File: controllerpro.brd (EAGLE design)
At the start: 38.7 x 83.2 mm, 10 parts, among them IC1 MCP1703CB, IC2 741G3157DBVR, IC3 741G3157DBVR, IC4 741G3157DBVR, IC5 741G3157DBVR

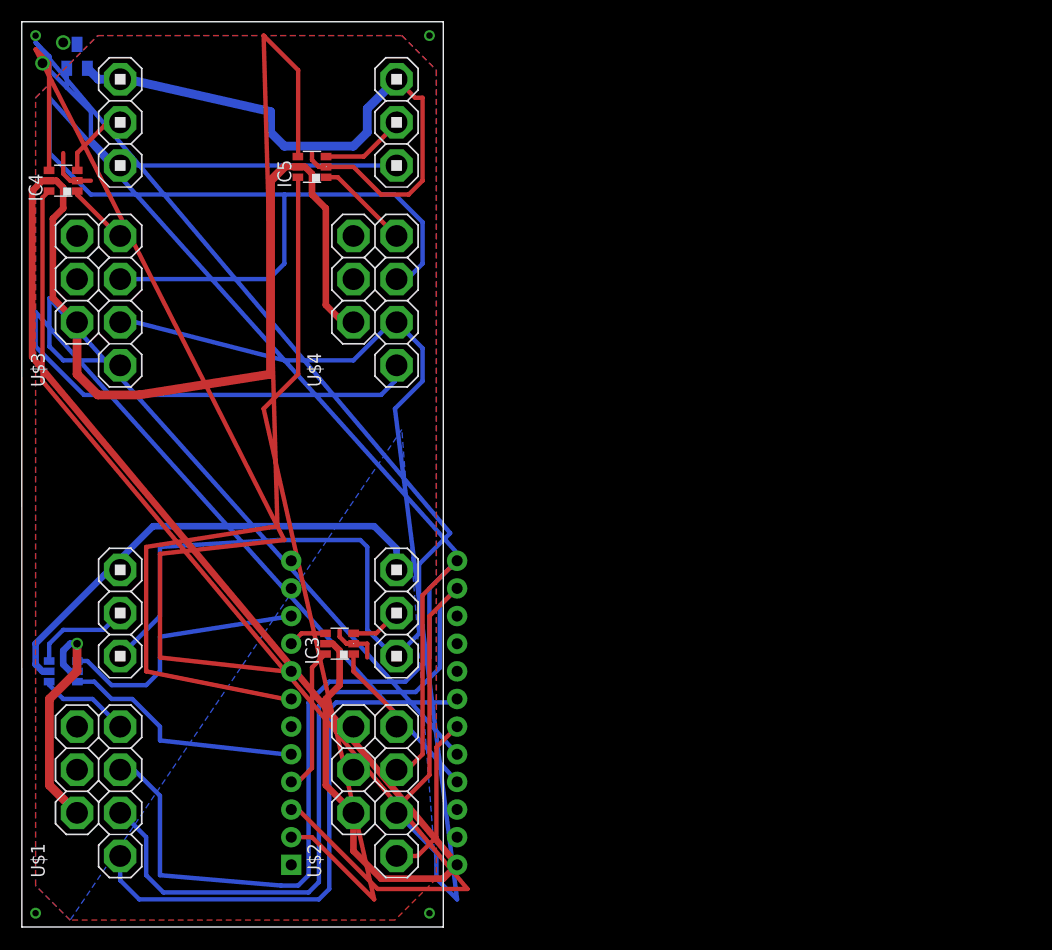
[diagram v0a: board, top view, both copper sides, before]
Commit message: Teensy in the middle of 2x2 (rotated)
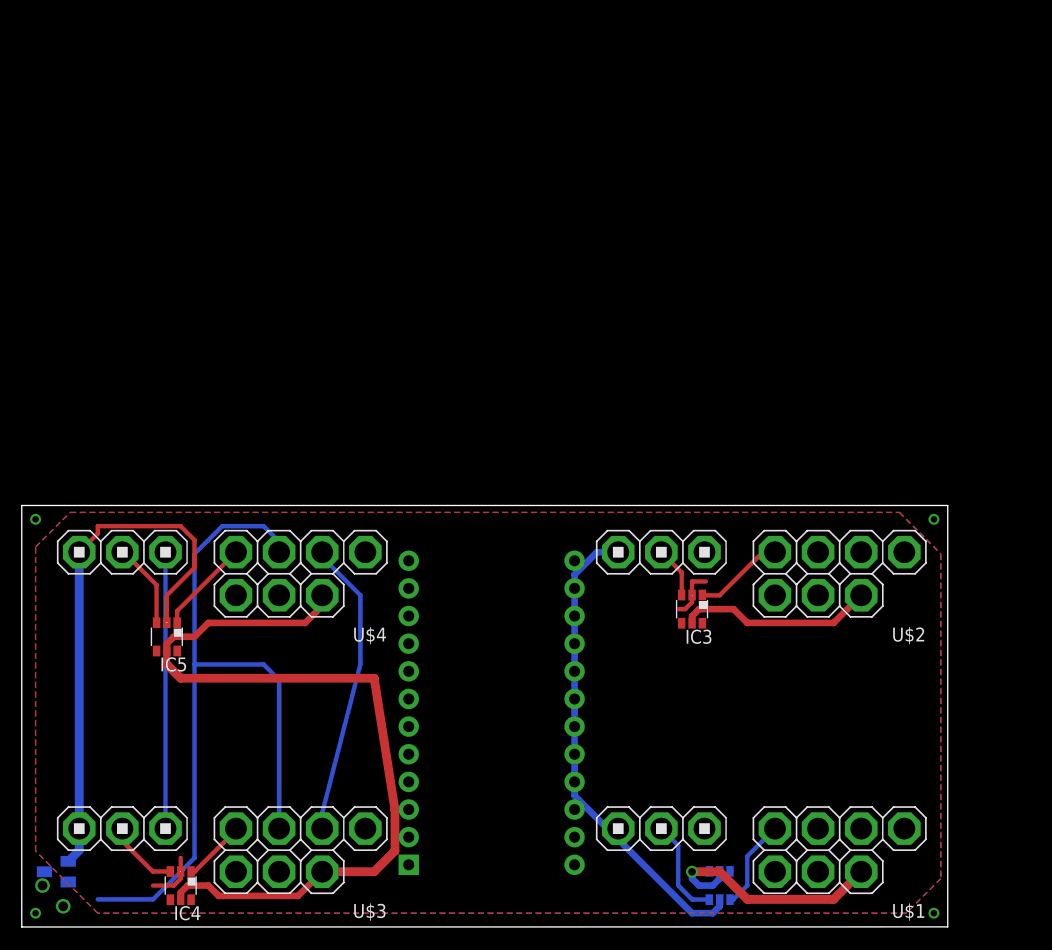
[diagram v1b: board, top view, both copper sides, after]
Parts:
- moved IC1 75.0 mm to (3.17, 5.08), turned to 270 degrees
- moved IC4 65.7 mm to (14.6, 3.81), turned to 180 degrees
- moved U$1 65.5 mm to (69.2, 5.08), turned to 180 degrees
- moved IC2 63.5 mm to (64.1, 3.81), turned to 0 degrees
- moved U$3 60.2 mm to (19.7, 5.08), turned to 180 degrees
- moved IC5 45.2 mm to (13.3, 26.7), turned to 180 degrees
- moved U$2 40.6 mm to (69.2, 30.5), turned to 180 degrees
- moved U$4 34.7 mm to (19.7, 30.5), turned to 180 degrees
- moved IC3 32.5 mm to (61.6, 29.2), turned to 180 degrees
- moved U$5 10.8 mm to (43.2, 19.7)
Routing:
- net CLOCK: track 176.4 -> 27.3 mm
- net LATCH: track 215.3 -> 70.8 mm
- net V33: track 156.4 -> 25.4 mm
- net S_OR_NES3: track 98.1 -> 0.00 mm
- net N64_OR_NES2: track 97.8 -> 0.00 mm
- net DATA2: track 95.3 -> 0.00 mm
- net DATA3: track 94.8 -> 0.00 mm
- net VCC: track 209.9 -> 117.3 mm
- net N64_OR_NES3: track 78.8 -> 0.00 mm
- net S_OR_NES2: track 67.9 -> 0.00 mm
- net S_OR_NES0: track 51.2 -> 0.00 mm
- net DATA0: track 24.4 -> 0.00 mm
- net N64_OR_NES0: track 22.7 -> 0.00 mm
- net S_OR_NES1: track 15.3 -> 0.00 mm
- net N64_OR_NES1: track 13.4 -> 0.00 mm
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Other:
- board size 38.7 x 83.2 mm -> 85.1 x 38.7 mm

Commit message: Using only needed pins
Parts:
- U$5: value TEENSY_HEADERS -> TEENSY_MC_PINS; device custom:TEENSY_HEADERS -> custom:TEENSY_MC_PINS
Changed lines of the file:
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@@
 <element name="IC4" library="74xx-little-de" package="DBV_R-PDSO-G6" value="741G3157DBVR" x="14.605" y="3.81" rot="R180"/>
 <element name="IC5" library="74xx-little-de" package="DBV_R-PDSO-G6" value="741G3157DBVR" x="13.335" y="26.67" rot="R180"/>
-<element name="U$5" library="custom" package="TEENSY_HEADERS" value="TEENSY_HEADERS" x="43.18" y="19.685" rot="MR90"/>
+<element name="U$5" library="custom" package="TEENSY_MC_PINS" value="TEENSY_MC_PINS" x="43.18" y="19.685" rot="MR90"/>
 </elements>
 <signals>

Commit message: All wired up (intially)!
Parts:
- moved IC1 39.4 mm to (42.5, 6.35), flipped to the top
- moved IC4 14.3 mm to (27.9, 8.89), turned to 270 degrees
- moved IC2 8.54 mm to (70.5, 9.53), flipped to the top
- moved IC3 5.43 mm to (56.5, 27.3), turned to 90 degrees
- moved U$1 4.96 mm to (66.0, 8.89), turned to 0 degrees
- moved U$3 4.96 mm to (16.5, 8.89), turned to 0 degrees
- moved U$2 3.24 mm to (68.6, 27.3)
- moved U$4 3.24 mm to (19.1, 27.3)
- moved IC5 0.90 mm to (14.0, 26.0)
- moved U$5 0.63 mm to (42.5, 19.7)
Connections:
- net DATA0: now also U$5.D2; no longer U$5.D3
- net DATA1: now also U$5.D3; no longer U$5.D2
- net DATA2: now also U$5.D0; no longer U$5.D1
- net DATA3: now also U$5.D1; no longer U$5.D0
- net N64_OR_NES0: now also U$5.B2; no longer U$5.B3
- net N64_OR_NES1: now also U$5.B3; no longer U$5.B2
- net N64_OR_NES2: now also U$5.B0; no longer U$5.B1
- net N64_OR_NES3: now also U$5.B1; no longer U$5.B0
- net S_OR_NES0: now also U$5.F6; no longer U$5.F7
- net S_OR_NES1: now also U$5.F7; no longer U$5.F6
- net S_OR_NES2: now also U$5.F4; no longer U$5.F5
- net S_OR_NES3: now also U$5.F5; no longer U$5.F4
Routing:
- net V33: track 25.4 -> 183.7 mm
- net CLOCK: track 27.3 -> 149.8 mm, vias 0 -> 1
- net LATCH: track 70.8 -> 159.4 mm
- net GND: track 104.0 -> 25.8 mm, vias 0 -> 2
- net S_OR_NES2: track 0.00 -> 63.6 mm, vias 0 -> 2
- net DATA0: track 0.00 -> 48.4 mm, vias 0 -> 1
- net VCC: track 117.3 -> 74.6 mm
- net N64_OR_NES3: track 0.00 -> 39.7 mm
- net N64_OR_NES0: track 0.00 -> 38.8 mm, vias 0 -> 1
- net S_OR_NES1: track 0.00 -> 37.5 mm
- net S_OR_NES3: track 0.00 -> 25.6 mm, vias 0 -> 1
- net N64_OR_NES1: track 0.00 -> 24.6 mm
- net DATA3: track 0.00 -> 24.4 mm
- net DATA1: track 0.00 -> 22.5 mm
- net DATA2: track 0.00 -> 19.4 mm, vias 0 -> 2
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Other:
- board size 85.1 x 38.7 mm -> 84.5 x 37.5 mm

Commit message: Trying to actually line up box with board
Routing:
- net GND: track 25.8 -> 24.0 mm
- net V33: track 183.7 -> 184.4 mm
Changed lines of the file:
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@@
 <wire x1="0" y1="0" x2="84.455" y2="0.01" width="0" layer="20"/>
 <wire x1="84.455" y1="0.01" x2="84.455" y2="37.465" width="0" layer="20"/>
+<dimension x1="51.435" y1="5.715" x2="33.655" y2="5.715" x3="42.545" y3="-4.444996875" textsize="1.778" layer="48" unit="inch" precision="4"/>
+<dimension x1="16.51" y1="8.89" x2="33.655" y2="8.89" x3="25.0825" y3="-5.08" textsize="1.778" layer="48" unit="inch" precision="4"/>
+<dimension x1="66.04" y1="8.89" x2="51.435" y2="8.89" x3="58.7375" y3="-4.445" textsize="1.778" layer="48" unit="inch" precision="4"/>
+<dimension x1="66.04" y1="8.89" x2="84.455" y2="8.89" x3="75.2475" y3="-4.445" textsize="1.778" layer="48" unit="inch" precision="4"/>
+<dimension x1="16.51" y1="8.89" x2="0" y2="8.89" x3="8.255" y3="-4.445" textsize="1.778" layer="48" unit="inch" precision="4"/>
+<dimension x1="16.51" y1="8.89" x2="42.545" y2="8.89" x3="29.5275" y3="-12.7" textsize="1.778" layer="48" unit="inch" precision="4"/>
+<dimension x1="19.05" y1="27.305" x2="42.545" y2="27.305" x3="30.7975" y3="43.18" textsize="1.778" layer="48" unit="inch" precision="4"/>
+<dimension x1="66.04" y1="8.89" x2="42.545" y2="8.89" x3="54.2925" y3="-12.7" textsize="1.778" layer="48" dtype="vertical" unit="inch" precision="4"/>
+<dimension x1="68.58" y1="27.305" x2="42.545" y2="27.305" x3="55.5625" y3="43.18" textsize="1.778" layer="48" dtype="vertical" unit="inch" precision="4"/>
+<dimension x1="16.51" y1="8.89" x2="42.545" y2="18.7325" x3="26.035" y3="13.81125" textsize="1.778" layer="48" dtype="vertical" unit="inch" precision="4"/>
+<dimension x1="42.545" y1="18.7325" x2="68.58" y2="27.305" x3="56.515" y3="23.01875" textsize="1.778" layer="48" dtype="vertical" unit="inch" precision="4"/>
 </plain>
 <attributes>
@@
 <vertex x="83.185" y="34.29"/>
 </polygon>
-<wire x1="80.01" y1="6.35" x2="80.01" y2="5.3594" width="0.6096" layer="16"/>
-<wire x1="80.01" y1="5.3594" x2="80.4418" y2="4.9276" width="0.6096" layer="16"/>
-<wire x1="81.28" y1="5.08" x2="80.5942" y2="5.08" width="0.6096" layer="16"/>
-<wire x1="80.5942" y1="5.08" x2="80.4418" y2="4.9276" width="0.4064" layer="16"/>
 <contactref element="U$5" pad="GND"/>
 <wire x1="13.97" y1="27.325" x2="13.97" y2="29.21" width="0.8128" layer="1"/>
-<wire x1="54.1782" y1="31.2674" x2="54.1782" y2="30.9118" width="0.6096" layer="1"/>
-<wire x1="54.1782" y1="30.9118" x2="56.515" y2="28.575" width="0.6096" layer="1"/>
-<wire x1="56.515" y1="28.575" x2="56.515" y2="27.94" width="0.6096" layer="1"/>
-<wire x1="56.515" y1="27.94" x2="57.15" y2="27.305" width="0.6096" layer="1"/>
-<wire x1="57.15" y1="27.305" x2="57.805" y2="27.305" width="0.6096" layer="1"/>
 <wire x1="70.485" y1="8.235" x2="70.485" y2="6.985" width="0.6096" layer="1"/>
 <wire x1="70.485" y1="6.985" x2="69.85" y2="6.35" width="0.6096" layer="1"/>
 <wire x1="26.65" y1="8.89" x2="27.305" y2="8.89" width="0.6096" layer="1"/>
 <wire x1="27.305" y1="8.89" x2="27.94" y2="8.255" width="0.6096" layer="1"/>
-<wire x1="27.94" y1="8.255" x2="27.94" y2="7.62" width="0.6096" layer="1"/>
-<wire x1="27.94" y1="7.62" x2="30.48" y2="5.08" width="0.6096" layer="1"/>
-<wire x1="30.48" y1="5.08" x2="30.7594" y2="5.08" width="0.6096" layer="1"/>
-<wire x1="30.7594" y1="5.08" x2="30.9118" y2="4.9276" width="0.6096" layer="1"/>
 <via x="41.275" y="27.94" extent="1-16" drill="0.7"/>
 <via x="46.355" y="22.86" extent="1-16" drill="0.7"/>
 <wire x1="41.275" y1="27.94" x2="46.355" y2="22.86" width="0.6096" layer="16"/>
+<wire x1="27.94" y1="8.255" x2="27.94" y2="6.985" width="0.6096" layer="1"/>
+<wire x1="27.94" y1="6.985" x2="29.845" y2="5.08" width="0.6096" layer="1"/>
+<wire x1="29.845" y1="5.08" x2="30.6324" y2="5.08" width="0.6096" layer="1"/>
+<wire x1="30.6324" y1="5.08" x2="30.7848" y2="4.9276" width="0.6096" layer="1"/>
+<wire x1="57.805" y1="27.305" x2="57.15" y2="27.305" width="0.6096" layer="1"/>
+<wire x1="57.15" y1="27.305" x2="56.515" y2="27.94" width="0.6096" layer="1"/>
+<wire x1="56.515" y1="27.94" x2="56.515" y2="29.845" width="0.6096" layer="1"/>
+<wire x1="56.515" y1="29.845" x2="55.245" y2="31.115" width="0.6096" layer="1"/>
+<wire x1="55.245" y1="31.115" x2="54.4576" y2="31.115" width="0.6096" layer="1"/>
+<wire x1="54.4576" y1="31.115" x2="54.3052" y2="31.2674" width="0.6096" layer="1"/>
 </signal>
 <signal name="V33">
@@
 <contactref element="U$4" pad="5"/>
 <contactref element="IC1" pad="2"/>
-<wire x1="12.573" y1="31.2674" x2="12.5476" y2="31.2674" width="0.4064" layer="16"/>
-<wire x1="12.065" y1="30.48" x2="12.065" y2="21.59" width="0.6096" layer="16"/>
+<wire x1="12.065" y1="30.6324" x2="12.065" y2="21.59" width="0.6096" layer="16"/>
 <wire x1="12.065" y1="21.59" x2="1.5875" y2="11.1125" width="0.6096" layer="16"/>
 <wire x1="1.5875" y1="11.1125" x2="1.5875" y2="3.4925" width="0.6096" layer="16"/>
 <wire x1="1.5875" y1="3.4925" x2="3.4925" y2="1.5875" width="0.6096" layer="16"/>
 <wire x1="3.4925" y1="1.5875" x2="19.6469" y2="1.5875" width="0.6096" layer="16"/>
-<wire x1="19.6469" y1="1.5875" x2="22.987" y2="4.9276" width="0.6096" layer="16"/>
+<wire x1="19.6469" y1="1.5875" x2="22.86" y2="4.445" width="0.6096" layer="16"/>
+<wire x1="22.86" y1="4.445" x2="22.86" y2="4.9276" width="0.6096" layer="16"/>
 <wire x1="41.445" y1="5.4" x2="40.325" y2="5.4" width="0.6096" layer="1"/>
 <wire x1="40.325" y1="5.4" x2="37.465" y2="2.54" width="0.6096" layer="1"/>
 <wire x1="37.465" y1="2.54" x2="25.3746" y2="2.54" width="0.6096" layer="1"/>
-<wire x1="25.3746" y1="2.54" x2="22.987" y2="4.9276" width="0.6096" layer="1"/>
-<wire x1="62.103" y1="31.2674" x2="62.103" y2="30.988" width="0.6096" layer="16"/>
-<wire x1="62.103" y1="30.988" x2="59.69" y2="28.575" width="0.6096" layer="16"/>
-<wire x1="59.69" y1="28.575" x2="49.53" y2="28.575" width="0.6096" layer="16"/>
+<wire x1="25.3746" y1="2.54" x2="23.495" y2="4.445" width="0.6096" layer="1"/>
+<wire x1="23.495" y1="4.445" x2="23.0124" y2="4.9276" width="0.6096" layer="1"/>
+<wire x1="23.0124" y1="4.9276" x2="22.86" y2="4.9276" width="0.6096" layer="1"/>
+<wire x1="60.325" y1="28.575" x2="49.53" y2="28.575" width="0.6096" layer="16"/>
 <wire x1="49.53" y1="28.575" x2="43.18" y2="34.925" width="0.6096" layer="16"/>
 <wire x1="43.18" y1="34.925" x2="16.2306" y2="34.925" width="0.6096" layer="16"/>
-<wire x1="16.2306" y1="34.925" x2="12.573" y2="31.2674" width="0.6096" layer="16"/>
-<wire x1="72.517" y1="4.9276" x2="72.517" y2="4.572" width="0.6096" layer="16"/>
-<wire x1="72.517" y1="4.572" x2="69.85" y2="1.905" width="0.6096" layer="16"/>
 <wire x1="69.85" y1="1.905" x2="26.0096" y2="1.905" width="0.6096" layer="16"/>
-<wire x1="26.0096" y1="1.905" x2="22.987" y2="4.9276" width="0.6096" layer="16"/>
-<wire x1="12.5476" y1="31.2674" x2="12.5476" y2="30.9626" width="0.6096" layer="16"/>
-<wire x1="12.5476" y1="30.9626" x2="12.065" y2="30.48" width="0.6096" layer="16"/>
+<wire x1="26.0096" y1="1.905" x2="23.495" y2="4.445" width="0.6096" layer="16"/>
+<wire x1="23.495" y1="4.445" x2="23.0124" y2="4.9276" width="0.6096" layer="16"/>
+<wire x1="23.0124" y1="4.9276" x2="22.86" y2="4.9276" width="0.6096" layer="16"/>
+<wire x1="12.065" y1="30.6324" x2="12.7" y2="31.2674" width="0.6096" layer="16"/>
+<wire x1="12.7" y1="31.2674" x2="12.7" y2="31.3944" width="0.6096" layer="16"/>
+<wire x1="12.7" y1="31.3944" x2="16.2306" y2="34.925" width="0.6096" layer="16"/>
+<wire x1="69.85" y1="1.905" x2="72.39" y2="4.445" width="0.6096" layer="16"/>
+<wire x1="72.39" y1="4.445" x2="72.39" y2="4.9276" width="0.6096" layer="16"/>
+<wire x1="60.325" y1="28.575" x2="62.23" y2="30.48" width="0.6096" layer="16"/>
+<wire x1="62.23" y1="30.48" x2="62.23" y2="31.2674" width="0.6096" layer="16"/>
 </signal>
 <signal name="N$5">
@@
 <contactref element="IC5" pad="3"/>
 <contactref element="U$4" pad="6"/>
-<wire x1="8.6106" y1="31.2674" x2="8.6106" y2="30.7594" width="0.4064" layer="1"/>
-<wire x1="8.6106" y1="30.7594" x2="12.065" y2="27.305" width="0.4064" layer="1"/>
 <wire x1="12.065" y1="27.305" x2="13" y2="27.305" width="0.4064" layer="1"/>
 <wire x1="13" y1="27.305" x2="13.02" y2="27.325" width="0.4064" layer="1"/>
+<wire x1="12.065" y1="27.305" x2="8.89" y2="30.48" width="0.4064" layer="1"/>
+<wire x1="8.89" y1="30.48" x2="8.89" y2="31.115" width="0.4064" layer="1"/>
+<wire x1="8.89" y1="31.115" x2="8.7376" y2="31.2674" width="0.4064" layer="1"/>
 </signal>
 <signal name="N$8">
@@
 <contactref element="U$1" pad="6"/>
 <wire x1="71.435" y1="8.235" x2="73.172" y2="8.235" width="0.4064" layer="1"/>
-<wire x1="73.172" y1="8.235" x2="76.4794" y2="4.9276" width="0.4064" layer="1"/>
+<wire x1="73.172" y1="8.235" x2="73.172" y2="8.108" width="0.4064" layer="1"/>
+<wire x1="73.172" y1="8.108" x2="76.3524" y2="4.9276" width="0.4064" layer="1"/>
 </signal>
 <signal name="N$9">
@@
 <contactref element="U$2" pad="6"/>
 <wire x1="57.805" y1="28.255" x2="57.805" y2="30.9318" width="0.4064" layer="1"/>
-<wire x1="57.805" y1="30.9318" x2="58.1406" y2="31.2674" width="0.4064" layer="1"/>
+<wire x1="57.805" y1="30.9318" x2="57.932" y2="30.9318" width="0.4064" layer="1"/>
+<wire x1="57.932" y1="30.9318" x2="58.2676" y2="31.2674" width="0.4064" layer="1"/>
 </signal>
 <signal name="N64_OR_NES0">
@@
 <contactref element="IC4" pad="3"/>
 <contactref element="U$3" pad="6"/>
-<wire x1="26.65" y1="7.94" x2="26.65" y2="5.227" width="0.4064" layer="1"/>
-<wire x1="26.65" y1="5.227" x2="26.9494" y2="4.9276" width="0.4064" layer="1"/>
+<wire x1="26.65" y1="7.94" x2="26.65" y2="5.1" width="0.4064" layer="1"/>
+<wire x1="26.65" y1="5.1" x2="26.8224" y2="4.9276" width="0.4064" layer="1"/>
 </signal>
 <signal name="N$15">
@@
 </signal>
 </signals>
-<errors>
-</errors>
 </board>
 </drawing>

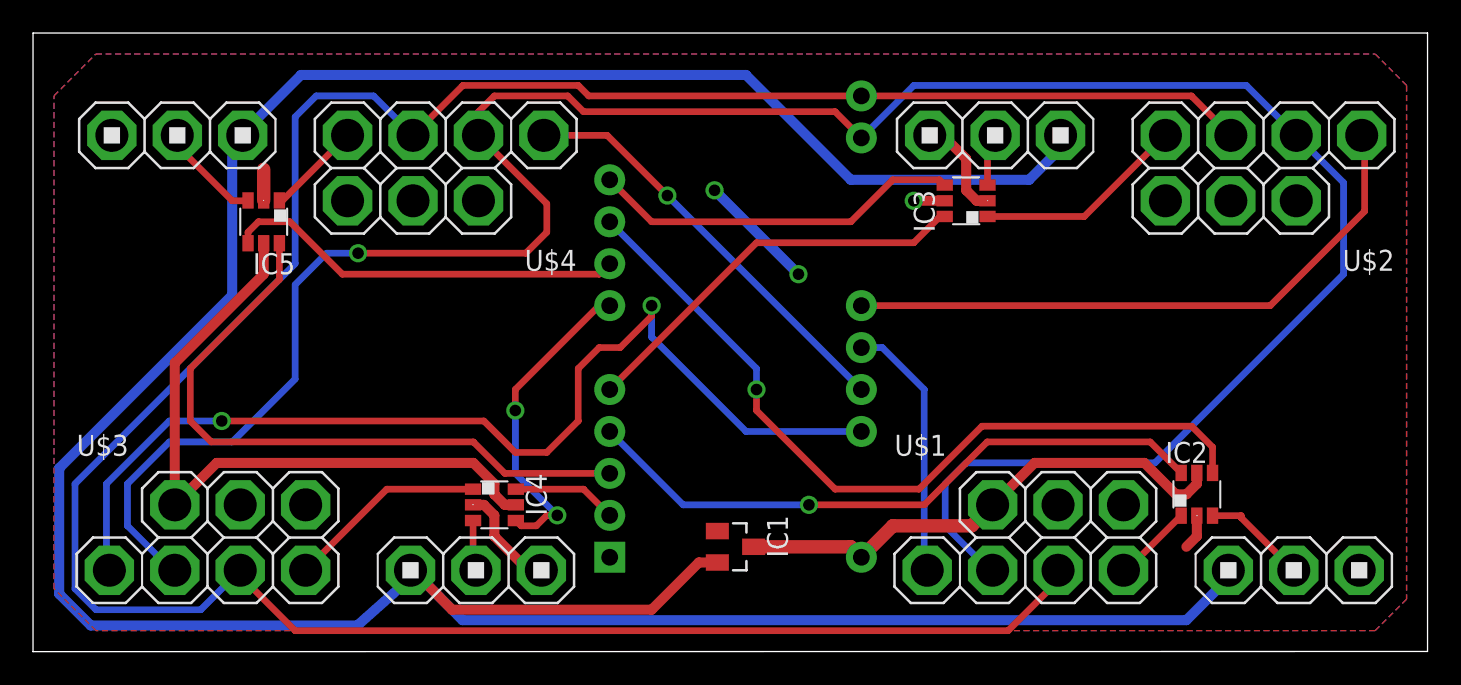
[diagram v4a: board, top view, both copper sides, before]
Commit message: Rerouting some stuff to shrink and center board
Updating model with new board dimensions and finishing
re-specfiying controller positions.  Yay!
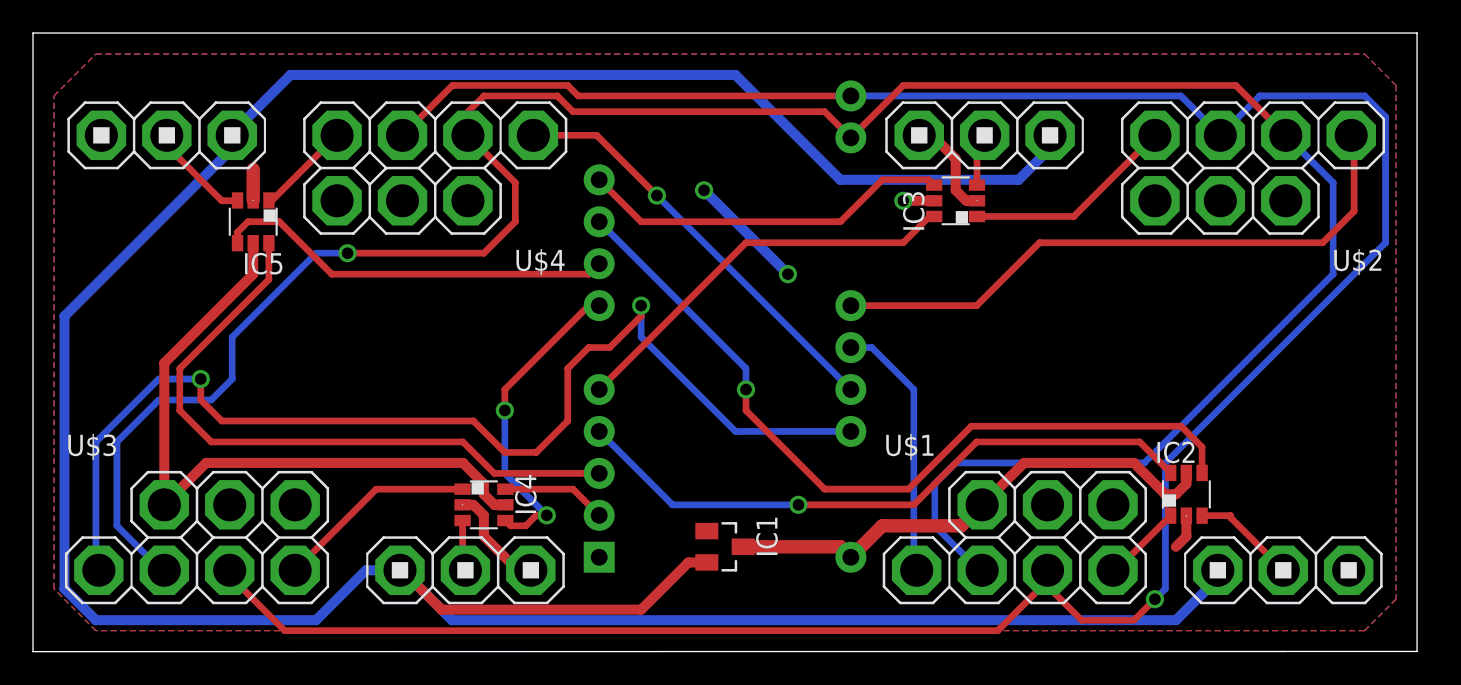
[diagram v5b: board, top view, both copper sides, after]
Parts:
- moved IC1 0.64 mm to (41.9, 6.35)
- moved IC2 0.64 mm to (69.8, 9.53)
- moved U$1 0.64 mm to (65.4, 8.89)
- moved U$2 0.64 mm to (67.9, 27.3)
- moved U$5 0.64 mm to (41.9, 19.7)
- moved IC4 0.64 mm to (27.3, 8.89)
- moved U$3 0.64 mm to (15.9, 8.89)
- moved U$4 0.64 mm to (18.4, 27.3)
- moved IC5 0.63 mm to (13.3, 26.0)
- moved IC3 0.63 mm to (55.9, 27.3)
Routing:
- net S_OR_NES2: track 63.6 -> 67.9 mm
- net CLOCK: track 149.8 -> 147.3 mm
- net V33: track 184.4 -> 182.4 mm
- net LATCH: track 159.4 -> 159.8 mm, vias 0 -> 1
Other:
- board size 84.5 x 37.5 mm -> 83.8 x 37.5 mm
